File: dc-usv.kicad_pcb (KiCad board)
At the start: 4 copper layers, 120 x 100 mm, 336 parts, among them J1 Output 2.0mm, J10 I2C, J2 Output 2.0mm, J3 Output 2.0mm, J4 SMBUS, J5 HanRun_HR911105A, J6 USB_C_Receptacle_USB2.0, J7 Input 2.0mm, J8 Input 2.5mm, J9 USB_C_Receptacle_USB2.0, Q1 AON7544, Q10 AO4407A, Q11 2N7002, Q12 MMBT3904, Q13 2N7002, Q14 2N7002, Q15 2N7002, Q16 2N7002, Q17 2N7002, Q18 MMBT3904, Q19 AO4407A, Q2 AO3401A, Q20 2N7002, Q21 AO4407A, Q22 2N7002, Q23 AO4407A, Q24 2N7002, Q25 AO3401A, Q26 2N7002, Q28 MMBT3904, Q29 MMBT3904, Q3 AON7544, Q30 MMBT3904, Q31 2N7002, Q32 AO4407A, Q33 MMBT3904, Q34 2N7002, Q35 AO4407A, Q36 MMBT3904, Q37 2N7002, Q38 AO4407A, Q4 AON7544, Q5 AON7544, Q6 CSD17308Q3, Q7 CSD17308Q3, Q8 AO4407A, Q9 2N7002, SW1 SW_DIP_x02, SW2 SW_Push, U1 BQ40z50-R2, U10 LAN8720A, U11 74HC595, U12 SY8105, U13 LM75B, U14 INA219AxD, U15 INA219AxD, U16 CH340C, U17 N066-6448TSWEG03-H28, U18 SRV05-4, U2 LM75B, U3 BQ24715, U4 TPS61178x, U5 INA219AxD, U6 INA219AxD, U7 LM75B, U8 SY8120B1ABC, U9 ESP32-WROOM-32E, Y1 12MHz (DNP)

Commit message: Add 3d models
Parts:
- added PANEL1: Frontpanel, Panels:Frontpanel, F.Cu at (140.0, 120.0)
- added PANEL2: Backpanel, Panels:Backpanel, F.Cu at (20.0, 20.0)

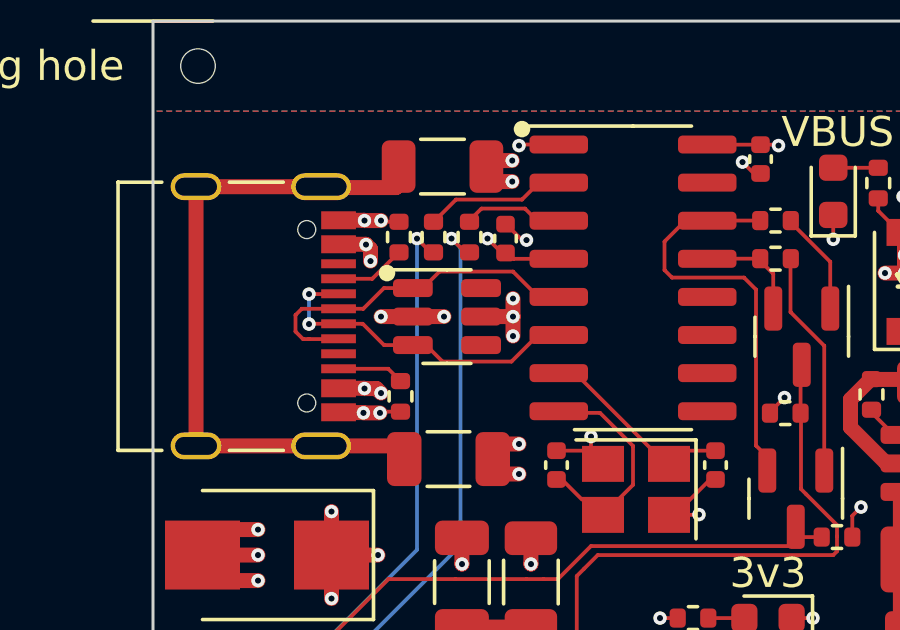
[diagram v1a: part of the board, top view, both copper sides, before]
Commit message: Fix reversed debug USB TVS
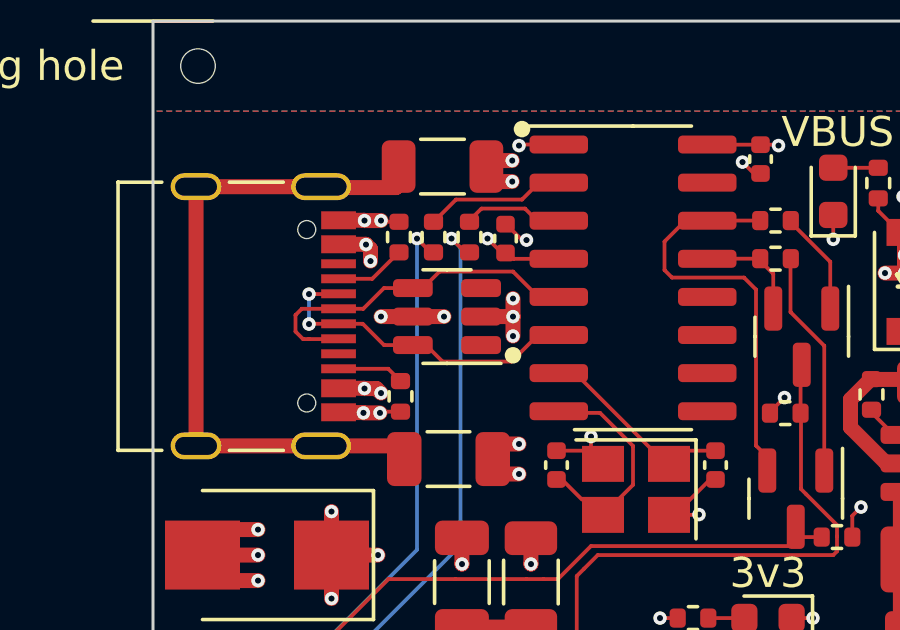
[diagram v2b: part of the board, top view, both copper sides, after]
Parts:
- turned U18 to 180 degrees
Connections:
- U18 pad 1: Net-(J9-PadA6) -> unconnected-(U18-Pad1)
- U18 pad 2: VBUS -> GND
- U18 pad 3: Net-(J9-PadA7) -> unconnected-(U18-Pad3)
- U18 pad 4: unconnected-(U18-Pad4) -> Net-(J9-PadA6)
- U18 pad 5: GND -> VBUS
- U18 pad 6: unconnected-(U18-Pad6) -> Net-(J9-PadA7)

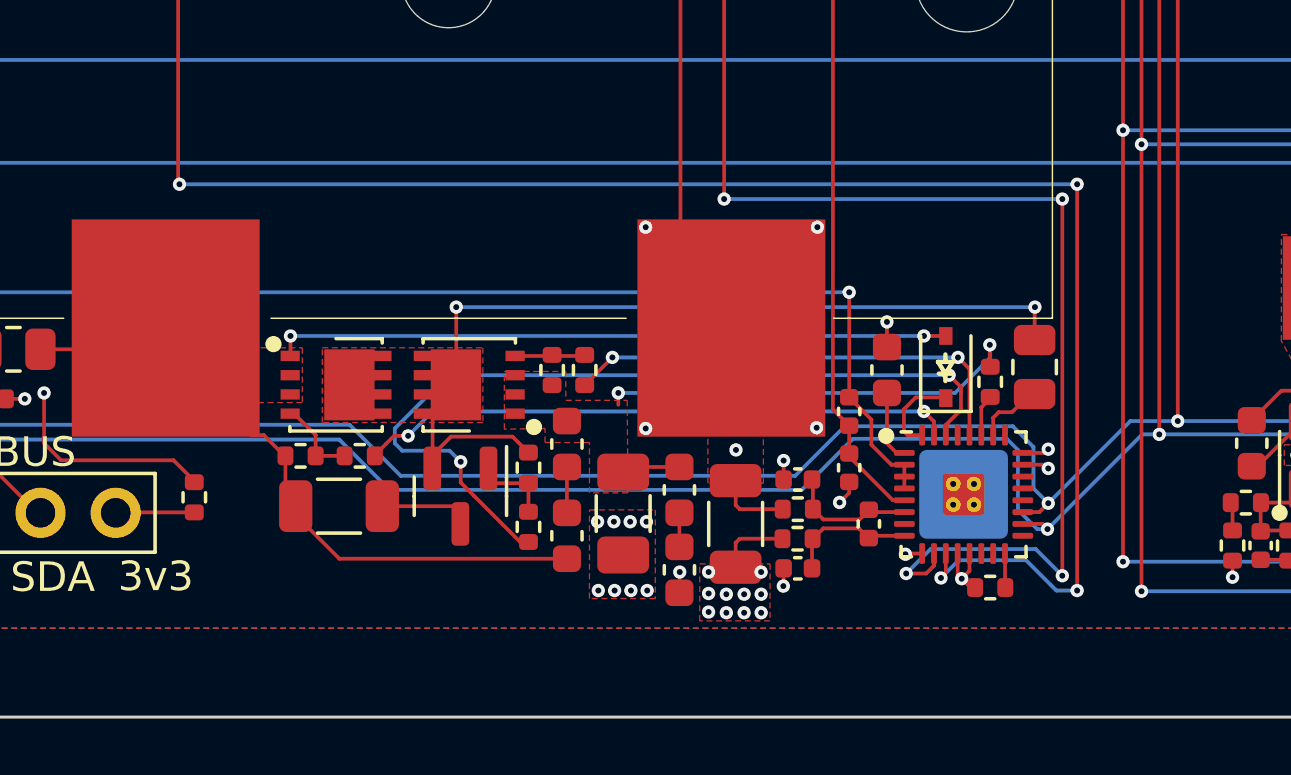
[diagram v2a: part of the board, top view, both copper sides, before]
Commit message: Add FUSE pulldown and PTC dummy
In contrast to documentation provided by TI FUSE is neither just an
output nor does the PTCEN feature work as advertised.

The FUSE pin contains a switchable 150nA current source. Presumably it
is used as a safety to detect if the FUSE pin is open. Unfortunately the
gauage will not allow control of the CHG, DSG and PRECHG FETs when it
detects an open FUSE pin. There does not seem to be any configuration
option for this behaviour either.

The PTC pin allows connecting a PTC to detect overheating of the main
power path control FETs. According to the BQ40Z50 datasheet it is possible
to disable this safety function by tieing PTCEN to VSS. Unfortunately this
does not seem to work as intended. When tieing both PTCEN and PTC to VSS
the gauage does not give any indication of a failure but refuses to switch
any of CHG, PRECHG or DSG FETs.
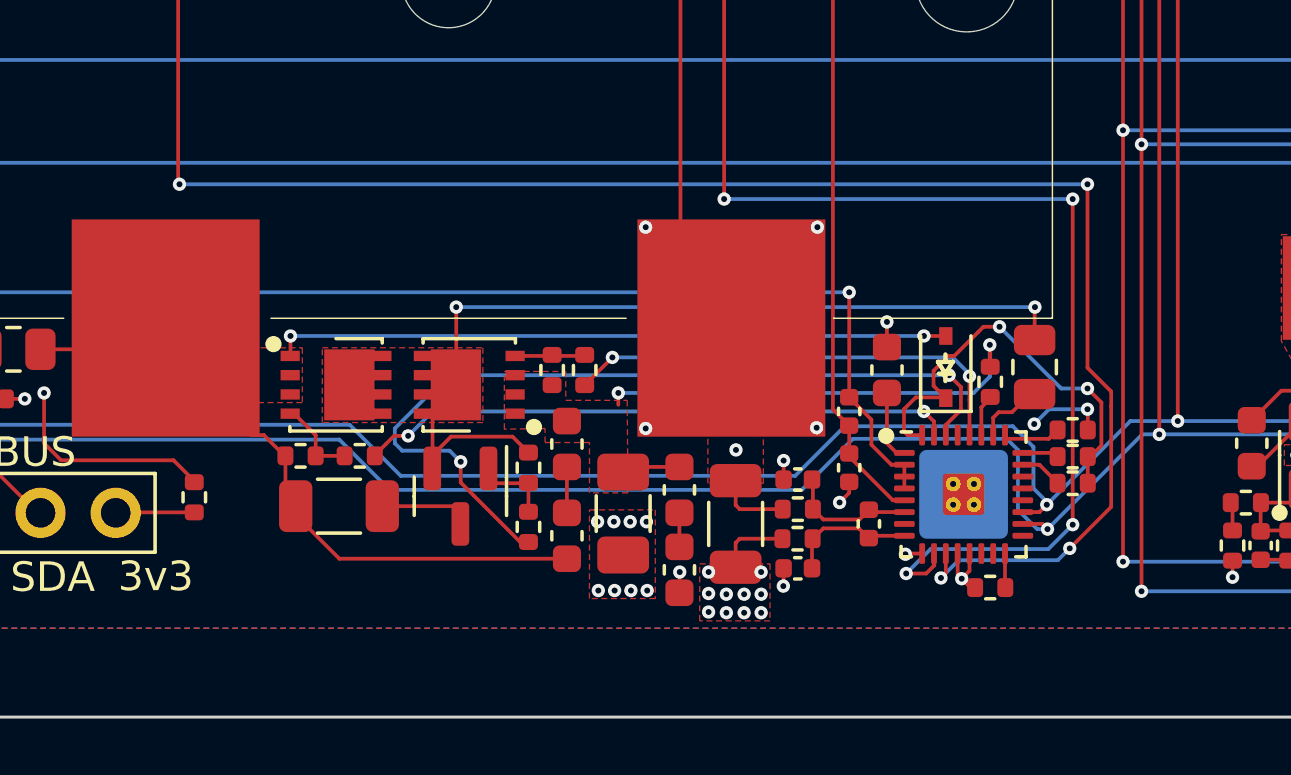
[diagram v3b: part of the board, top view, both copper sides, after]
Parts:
- added R128: 10k, Resistor_SMD:R_0402_1005Metric, F.Cu at (95.1, 110.3)
- added R129: 10k, Resistor_SMD:R_0402_1005Metric, F.Cu at (95.1, 112.1)
- added R130: 100R, Resistor_SMD:R_0402_1005Metric, F.Cu at (95.1, 111.2)
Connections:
- net Net-(D1-Pad1) renamed /Battery Pack/BAT
- U1 pad 23: GND1 -> Net-(U1-Pad23)
- U1 pad 24: GND1 -> Net-(U1-Pad24)
- U1 pad 25: unconnected-(U1-Pad25) -> Net-(U1-Pad25)
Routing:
- net /Battery Pack/BAT: track 2.98 -> 14.5 mm, vias 0 -> 2
- net Net-(U1-Pad25): track 0.00 -> 1.91 mm
- net Net-(U1-Pad23): track 0.00 -> 1.44 mm
- net Net-(U1-Pad24): track 0.00 -> 1.24 mm
- net Net-(TH1-Pad2): track 65.0 -> 64.0 mm
- net GND1: track 64.5 -> 65.3 mm
- net /Battery Pack/VBAT: track 16.6 -> 17.4 mm
- net Net-(TH2-Pad2): track 83.2 -> 82.5 mm

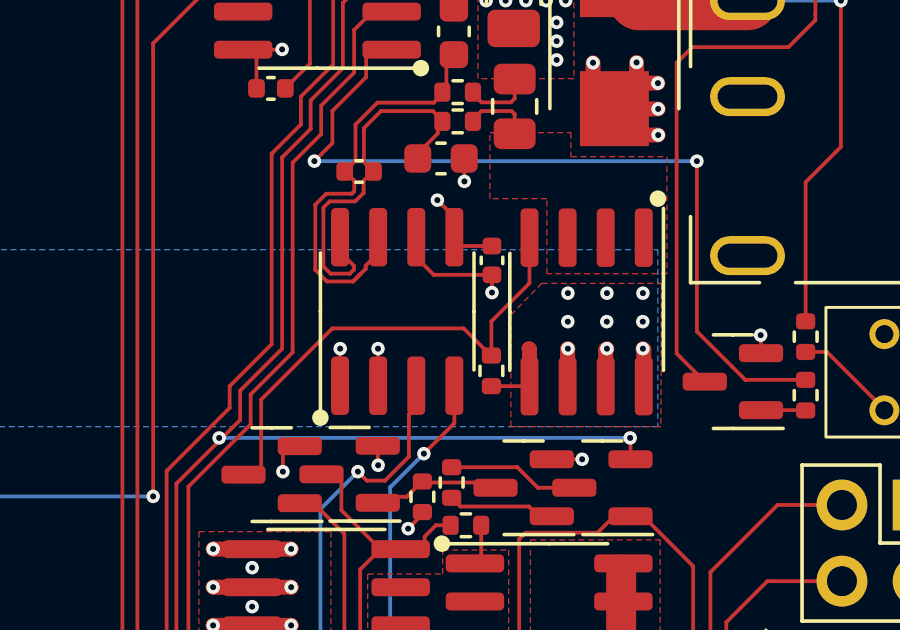
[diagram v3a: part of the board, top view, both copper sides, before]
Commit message: Fix gate discharge resistor on Q10
The gate discharge resistor on Q10 was by mistake connected to drain
instead of source.
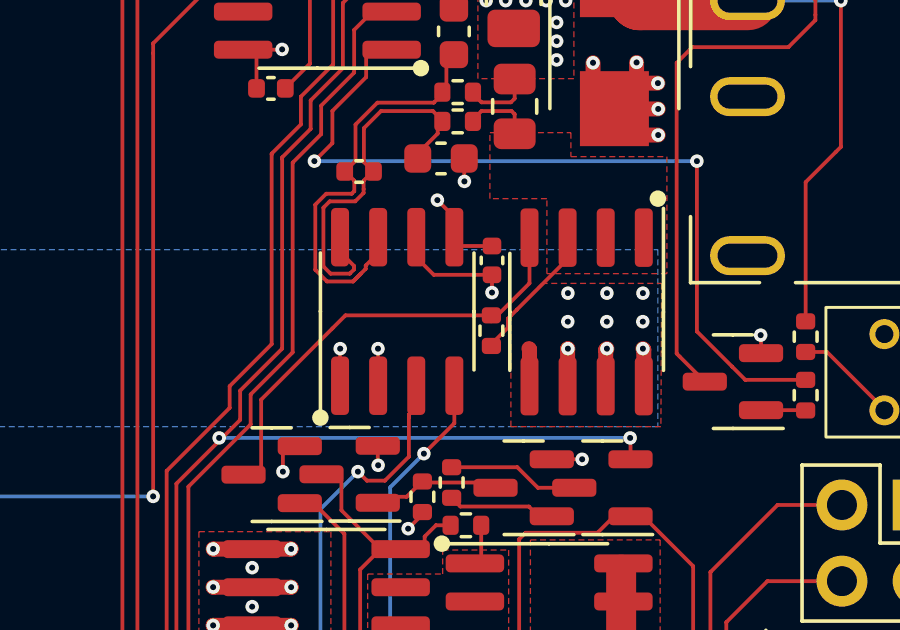
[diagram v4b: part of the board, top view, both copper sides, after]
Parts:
- moved R26 1.34 mm to (122.2, 67.3), turned to 90 degrees
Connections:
- R26 pad 1: Net-(Q10-Pad4) -> /DC Control/DCTHRU
- R26 pad 2: /Charger/DCIN -> Net-(Q10-Pad4)
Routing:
- net /DC Control/DCTHRU: track 2.30 -> 6.97 mm
- net Net-(Q10-Pad4): track 16.4 -> 15.1 mm
- net /Charger/DCIN: track 25.0 -> 23.8 mm
